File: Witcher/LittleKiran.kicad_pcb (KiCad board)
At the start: 2 copper layers, 39 x 37 mm, 19 parts, among them J1 XT60PW-M, J2 XT60PW-M, J3 XT60PW-F, Q2 SQS141ELNW-T1_GE3, Q3 SQS141ELNW-T1_GE3, Q4 FDN340P, Q5 SQS141ELNW-T1_GE3, U1 LTC4412xS6, U2 LTC4412xS6

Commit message: v2.0
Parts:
- removed the Q5 at (138.3, 81.9)
- added G***: LOGO, iclr:iclr_logo_estd2018_6mm, F.Cu at (145.6, 98.5)
- added G***: LOGO, iclr:rae_logo_6mm, F.Cu at (145.7, 90.8)
- added G***: LOGO, iclr:rae_logo_6mm, B.Cu at (145.5, 98.3)
- added G***: LOGO, iclr:iclr_logo_estd2018_6mm, B.Cu at (138.0, 68.3)
- added J4: Conn_01x02_Pin, Connector_Molex:Molex_Nano-Fit_105313-xx02_1x02_P2.50mm_Horizontal, F.Cu at (116.2, 93.2)
- added Q2: SQS141ELNW-T1_GE3, iclr:SQS850ENT1_GE3, F.Cu at (123.0, 87.6)
- added Q3: SQS141ELNW-T1_GE3, iclr:SQS850ENT1_GE3, F.Cu at (138.4, 82.0)
- added R3: 10k, Resistor_SMD:R_0402_1005Metric, F.Cu at (131.4, 78.4)
- added R4: 10k, Resistor_SMD:R_0402_1005Metric, F.Cu at (128.3, 78.4)
- added R5: 10k, Resistor_SMD:R_0402_1005Metric, F.Cu at (128.3, 77.4)
- R1: value 0 -> 470k; footprint Resistor_SMD:R_0603_1608Metric -> Resistor_SMD:R_0402_1005Metric
- R2: footprint Resistor_SMD:R_0603_1608Metric -> Resistor_SMD:R_0402_1005Metric
- moved Q1 7.06 mm to (123.1, 82.0), turned to 90 degrees
- moved G*** 4.76 mm to (129.3, 85.2), turned to 0 degrees
- moved R1 4.52 mm to (131.4, 79.4)
- moved R2 3.72 mm to (131.4, 77.4), turned to 180 degrees
- moved U2 1.60 mm to (128.5, 82.6), turned to -90 degrees
- renumbered Q3 to Q1, Q2 to Q4, Q4 to Q5, R5 to R6, R4 to R7, R3 to R8
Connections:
- net Net-(J1-+) renamed VBAT
- net Net-(J2-+) renamed VADP
- net Net-(Q3-G) renamed /GATE2
- J3 pad 2: /SENSE -> VOUT
- J3 pad S2: unconnected-(J3-SHIELD-PadS1) -> unconnected-(J3-SHIELD-PadS1)_1
- Q1 pad 1: /SENSE -> Net-(Q1-Pad1)
- Q1 pad 2: /SENSE -> Net-(Q1-Pad1)
- Q1 pad 3: /SENSE -> Net-(Q1-Pad1)
- Q4 pad 10: /SENSE -> VOUT
- Q4 pad 11: /SENSE -> VOUT
- Q4 pad 5: /SENSE -> VOUT
- Q4 pad 6: /SENSE -> VOUT
- Q4 pad 7: /SENSE -> VOUT
- Q4 pad 8: /SENSE -> VOUT
- Q4 pad 9: /SENSE -> VOUT
- R7 pad 1: /SENSE -> VOUT
- R8 pad 1: /SENSE -> VOUT
- U1 pad 6: /SENSE -> VOUT
- U2 pad 3: GND -> Net-(U2-CTL)
- U2 pad 6: /SENSE -> VOUT
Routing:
- net VRST: track 0.00 -> 28.3 mm, vias 0 -> 1
- net /GATE2: track 4.19 -> 15.2 mm, vias 0 -> 2
- net VADP: track 0.00 -> 9.45 mm, vias 31 -> 29
- net Net-(U2-CTL): track 0.00 -> 4.14 mm
- net GND: track 4.05 -> 0.00 mm, vias 28 -> 26
- net Net-(U1-CTL): track 2.90 -> 4.47 mm
- net VOUT: vias 0 -> 44
- net Net-(Q1-Pad1): vias 0 -> 19
- net /SENSE: vias 31 -> 0
- added copper zone on B.Cu, net Net-(Q1-Pad1)
- added copper zone on F.Cu, net Net-(Q1-Pad1)
- added copper zone on B.Cu, net VOUT
- added copper zone on F.Cu, net VOUT
- removed copper zone on B.Cu, net /SENSE
- removed copper zone on F.Cu, net /SENSE
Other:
- board text added: "Designed by Artem Sheykin Andrei Paduraru Electronics 2024"
- board text added: "RESET"
- board text added: "v2.0"

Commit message: Simulation model
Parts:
- J4: footprint Connector_Molex:Molex_Nano-Fit_105313-xx02_1x02_P2.50mm_Horizontal -> iclr:Molex_Nano-Fit_105313-xx02_1x02_P2.50mm_Horizontal
- R3, R4: value 10k -> 1k
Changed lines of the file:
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@@
 		)
 	)
-	(footprint "Connector_Molex:Molex_Nano-Fit_105313-xx02_1x02_P2.50mm_Horizontal"
+	(footprint "iclr:Molex_Nano-Fit_105313-xx02_1x02_P2.50mm_Horizontal"
 		(layer "F.Cu")
 		(at 116.15 93.15 -90)
@@
 		(tags "connector Molex Nano-Fit top entry")
 		(property "Reference" "J4"
-			(at 6.15 -2.92 270)
+			(at 6.15 -2.92 -90)
 			(layer "F.SilkS")
-			(hide yes)
 			(effects
 				(font
@@
 			)
 		)
-		(property "Footprint" "Connector_Molex:Molex_Nano-Fit_105313-xx02_1x02_P2.50mm_Horizontal"
+		(property "Footprint" "iclr:Molex_Nano-Fit_105313-xx02_1x02_P2.50mm_Horizontal"
 			(at 0 0 -90)
 			(unlocked yes)
@@
 			(pintype "passive")
 		)
-		(model "${KICAD8_3DMODEL_DIR}/Connector_Molex.3dshapes/Molex_Nano-Fit_105313-xx02_1x02_P2.50mm_Horizontal.wrl"
+		(model "${ICLR_HW}/3d/1053131102.stp"
 			(offset
-				(xyz 0 0 0)
+				(xyz 6.15 -1.25 2)
 			)
 			(scale
@@
 			)
 			(rotate
-				(xyz 0 0 0)
+				(xyz -90 0 -90)
 			)
 		)
@@
 			)
 		)
-		(property "Value" "10k"
+		(property "Value" "1k"
 			(at 0 1.17 0)
 			(layer "F.Fab")
@@
 			)
 		)
-		(property "Value" "10k"
+		(property "Value" "1k"
 			(at 0 1.17 0)
 			(layer "F.Fab")

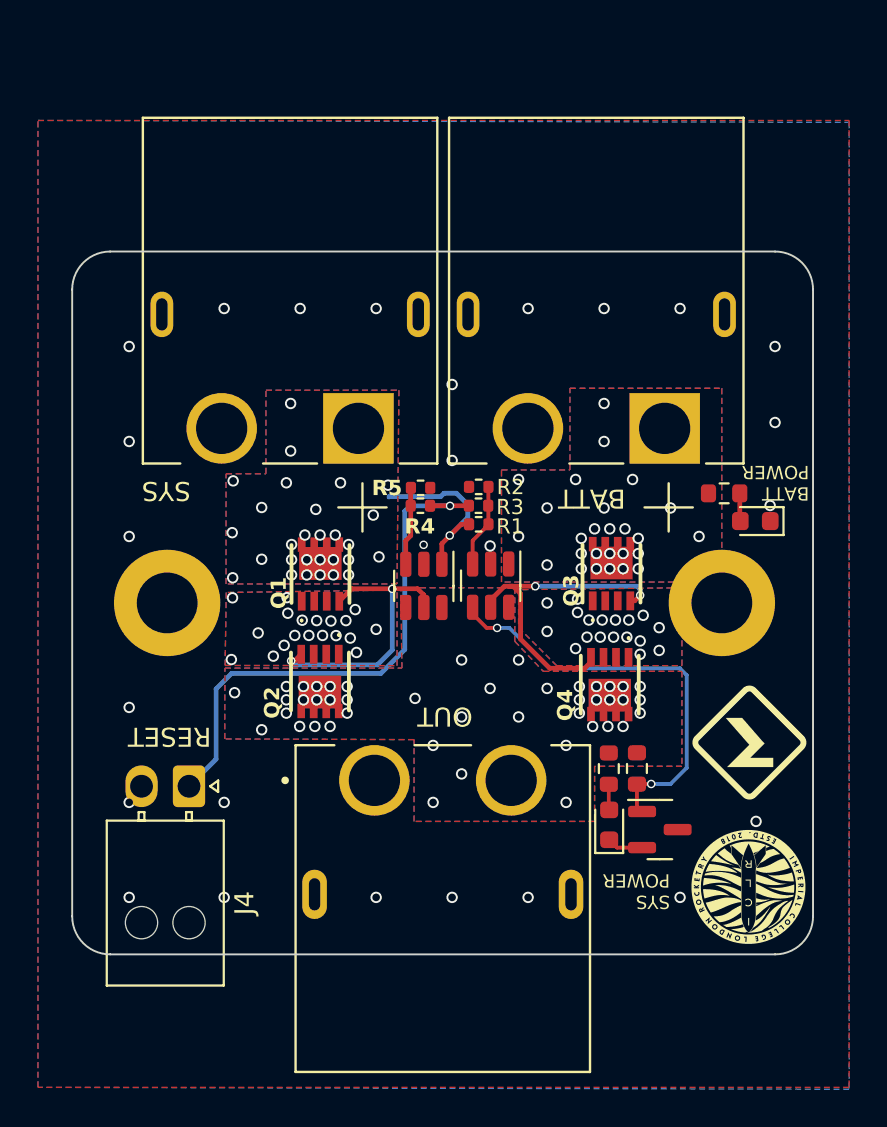
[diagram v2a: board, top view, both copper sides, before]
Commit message: Moved reset to the left
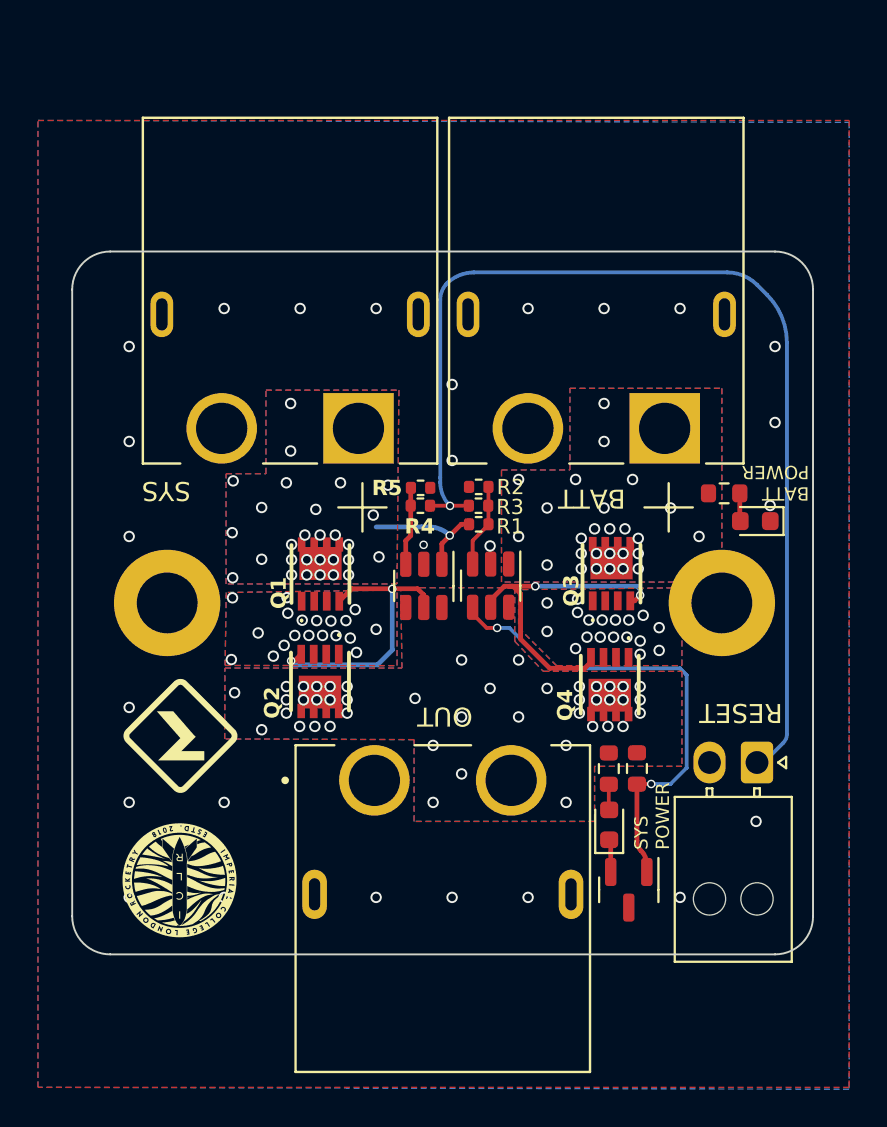
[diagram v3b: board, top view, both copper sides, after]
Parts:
- moved G*** 30.0 mm to (115.7, 90.5)
- moved G*** 30.0 mm to (115.7, 98.1)
- moved G*** 29.9 mm to (115.6, 98.0)
- moved J4 29.9 mm to (146.1, 91.9)
- moved Q5 3.57 mm to (139.3, 98.6), turned to -90 degrees
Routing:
- net VRST: track 28.3 -> 56.8 mm
- net /STAT: track 22.4 -> 25.6 mm
- net VADP: track 9.45 -> 6.93 mm

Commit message: somehow 4 layer was cheaper on JLC? I'll take it tho
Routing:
- added copper zone on In1.Cu, net GND
- added copper zone on In2.Cu, net GND
- added copper zone on In1.Cu, net Net-(Q1-Pad1)
- added copper zone on In2.Cu, net Net-(Q1-Pad1)
- added copper zone on In1.Cu, net Net-(Q3-Pad1)
- added copper zone on In2.Cu, net Net-(Q3-Pad1)
- added copper zone on In1.Cu, net VADP
- added copper zone on In2.Cu, net VADP
- added copper zone on In1.Cu, net VBAT
- added copper zone on In2.Cu, net VBAT
- added copper zone on In1.Cu, net VOUT
- added copper zone on In2.Cu, net VOUT
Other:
- copper layers 2 -> 4
- board text added: "JLCJLCJLCJLC"
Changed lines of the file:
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@@
 	(layers
 		(0 "F.Cu" signal)
+		(1 "In1.Cu" signal)
+		(2 "In2.Cu" signal)
 		(31 "B.Cu" signal)
 		(32 "B.Adhes" user "B.Adhesive")
@@
 			)
 			(layer "dielectric 1"
+				(type "prepreg")
+				(color "FR4 natural")
+				(thickness 0.1)
+				(material "FR4")
+				(epsilon_r 4.5)
+				(loss_tangent 0.02)
+			)
+			(layer "In1.Cu"
+				(type "copper")
+				(thickness 0.035)
+			)
+			(layer "dielectric 2"
 				(type "core")
 				(color "FR4 natural")
-				(thickness 1.51)
+				(thickness 1.24)
+				(material "FR4")
+				(epsilon_r 4.5)
+				(loss_tangent 0.02)
+			)
+			(layer "In2.Cu"
+				(type "copper")
+				(thickness 0.035)
+			)
+			(layer "dielectric 3"
+				(type "prepreg")
+				(color "FR4 natural")
+				(thickness 0.1)
 				(material "FR4")
 				(epsilon_r 4.5)
@@
 		(tags "connector Molex Nano-Fit top entry")
 		(property "Reference" "J4"
-			(at 6.15 -2.92 270)
+			(at 6.15 -2.92 -90)
 			(layer "F.SilkS")
 			(hide yes)
@@
 		)
 	)
+	(gr_text "JLCJLCJLCJLC\n"
+		(at 125.55 97.2 0)
+		(layer "F.SilkS")
+		(effects
+			(font
+				(size 0.8 0.8)
+				(thickness 0.1524)
+				(bold yes)
+			)
+			(justify left bottom)
+		)
+	)
 	(gr_text "OUT"
 		(at 129.625 89.475 180)
@@
 		(net 4)
 		(net_name "GND")
-		(layer "F.Cu")
+		(layers "F.Cu" "In1.Cu")
 		(hatch edge 0.508)
 		(connect_pads yes
@@
 		(net 17)
 		(net_name "Net-(Q3-Pad1)")
-		(layers "F&B.Cu")
+		(layers "F.Cu" "In1.Cu" "In2.Cu" "B.Cu")
 		(hatch edge 0.5)
 		(priority 4)
@@
 		(polygon
 			(pts
-				(xy 142.1 86.8) (xy 142.1 82.7) (xy 133.5 82.8) (xy 133.5 84.8) (xy 135.5 86.8)
+				(xy 142.1 86.8) (xy 142.1 82.7) (xy 133.5 82.8) (xy 133.5 85.3) (xy 134.975 86.775)
 			)
 		)
@@
 		(net 3)
 		(net_name "VADP")
-		(layers "F&B.Cu")
+		(layers "F.Cu" "In1.Cu" "In2.Cu" "B.Cu")
 		(hatch edge 0.5)
 		(priority 5)
@@
 		(net 14)
 		(net_name "VOUT")
-		(layers "F&B.Cu")
+		(layers "F.Cu" "In1.Cu" "In2.Cu" "B.Cu")
 		(hatch edge 0.5)
 		(priority 2)
@@
 		(net 16)
 		(net_name "Net-(Q1-Pad1)")
-		(layers "F&B.Cu")
+		(layers "F.Cu" "In1.Cu" "In2.Cu" "B.Cu")
 		(hatch edge 0.5)
 		(priority 4)
@@
 		(polygon
 			(pts
-				(xy 127.1 86.8) (xy 127.1 82.82) (xy 118.11 82.95) (xy 118.05 86.79)
+				(xy 127.075 86.8) (xy 127.075 82.82) (xy 118.11 82.95) (xy 118.05 86.79)
 			)
 		)
@@
 		(net 1)
 		(net_name "VBAT")
-		(layers "F&B.Cu")
+		(layers "F.Cu" "In1.Cu" "In2.Cu" "B.Cu")
 		(hatch edge 0.5)
 		(priority 3)
@@
 		(net 4)
 		(net_name "GND")
-		(layer "B.Cu")
+		(layers "In2.Cu" "B.Cu")
 		(hatch edge 0.508)
 		(priority 1)
